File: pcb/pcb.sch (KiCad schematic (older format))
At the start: 0 parts

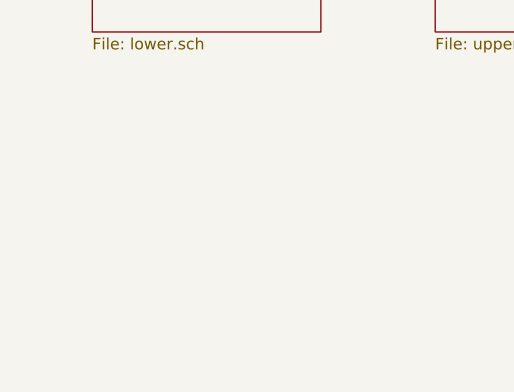
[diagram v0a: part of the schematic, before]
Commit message: Add tooling holes to schematic
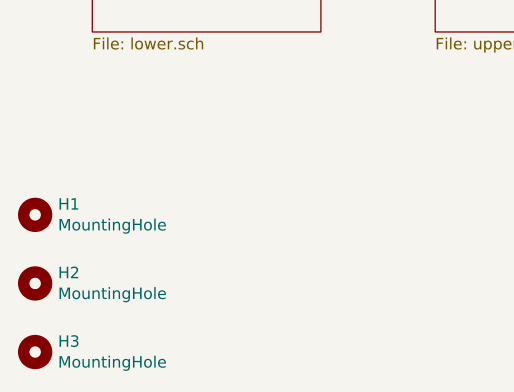
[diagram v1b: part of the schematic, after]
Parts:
- added H1, H2, H3: MountingHole, node:JLCPCB-tooling-hole, symbol Mechanical:MountingHole
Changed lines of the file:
@@
 F1 "upper.sch" 50
 $EndSheet
+$Comp
+L Mechanical:MountingHole H?
+U 1 1 5FB14092
+P 4250 4800
+AR Path="/5C920754/5FB14092" Ref="H?"  Part="1"
+AR Path="/5FB14092" Ref="H1"  Part="1"
+F 0 "H1" H 4350 4846 50  0000 L CNN
+F 1 "MountingHole" H 4350 4755 50  0000 L CNN
+F 2 "node:JLCPCB-tooling-hole" H 4250 4800 50  0001 C CNN
+F 3 "~" H 4250 4800 50  0001 C CNN
+	1    4250 4800
+	1    0    0    -1
+$EndComp
+$Comp
+L Mechanical:MountingHole H?
+U 1 1 5FB14098
+P 4250 5100
+AR Path="/5C920754/5FB14098" Ref="H?"  Part="1"
+AR Path="/5FB14098" Ref="H2"  Part="1"
+F 0 "H2" H 4350 5146 50  0000 L CNN
+F 1 "MountingHole" H 4350 5055 50  0000 L CNN
+F 2 "node:JLCPCB-tooling-hole" H 4250 5100 50  0001 C CNN
+F 3 "~" H 4250 5100 50  0001 C CNN
+	1    4250 5100
+	1    0    0    -1
+$EndComp
+$Comp
+L Mechanical:MountingHole H?
+U 1 1 5FB14457
+P 4250 5400
+AR Path="/5C920754/5FB14457" Ref="H?"  Part="1"
+AR Path="/5FB14457" Ref="H3"  Part="1"
+F 0 "H3" H 4350 5446 50  0000 L CNN
+F 1 "MountingHole" H 4350 5355 50  0000 L CNN
+F 2 "node:JLCPCB-tooling-hole" H 4250 5400 50  0001 C CNN
+F 3 "~" H 4250 5400 50  0001 C CNN
+	1    4250 5400
+	1    0    0    -1
+$EndComp
 $EndSCHEMATC

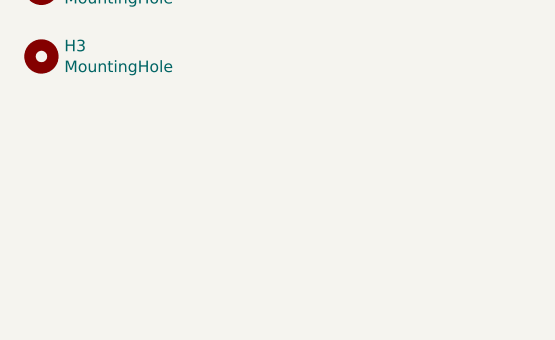
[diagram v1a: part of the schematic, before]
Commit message: Add mouse bite
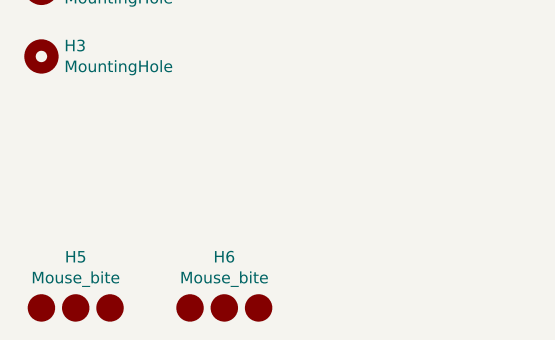
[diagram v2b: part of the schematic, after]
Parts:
- added H5, H6: Mouse_bite, node:single_sided_tab_5mm, symbol node:Mouse_bite
- H1, H2, H3: JLCPCB BOM (none) -> False
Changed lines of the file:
@@
 F 2 "node:JLCPCB-tooling-hole" H 4250 4800 50  0001 C CNN
 F 3 "~" H 4250 4800 50  0001 C CNN
+F 4 "False" H 4250 4800 50  0001 C CNN "JLCPCB BOM"
 	1    4250 4800
 	1    0    0    -1
@@
 F 2 "node:JLCPCB-tooling-hole" H 4250 5100 50  0001 C CNN
 F 3 "~" H 4250 5100 50  0001 C CNN
+F 4 "False" H 4250 5100 50  0001 C CNN "JLCPCB BOM"
 	1    4250 5100
 	1    0    0    -1
@@
 F 2 "node:JLCPCB-tooling-hole" H 4250 5400 50  0001 C CNN
 F 3 "~" H 4250 5400 50  0001 C CNN
+F 4 "False" H 4250 5400 50  0001 C CNN "JLCPCB BOM"
 	1    4250 5400
 	1    0    0    -1
 $EndComp
+$Comp
+L node:Mouse_bite H5
+U 1 1 5FB1D088
+P 4400 6500
+F 0 "H5" H 4400 6722 50  0000 C CNN
+F 1 "Mouse_bite" H 4400 6631 50  0000 C CNN
+F 2 "node:single_sided_tab_5mm" H 4400 6500 50  0001 C CNN
+F 3 "" H 4400 6500 50  0001 C CNN
+F 4 "False" H 4400 6500 50  0001 C CNN "JLCPCB BOM"
+	1    4400 6500
+	1    0    0    -1
+$EndComp
+$Comp
+L node:Mouse_bite H6
+U 1 1 5FB1D23F
+P 5050 6500
+F 0 "H6" H 5050 6722 50  0000 C CNN
+F 1 "Mouse_bite" H 5050 6631 50  0000 C CNN
+F 2 "node:single_sided_tab_5mm" H 5050 6500 50  0001 C CNN
+F 3 "" H 5050 6500 50  0001 C CNN
+F 4 "False" H 5050 6500 50  0001 C CNN "JLCPCB BOM"
+	1    5050 6500
+	1    0    0    -1
+$EndComp
